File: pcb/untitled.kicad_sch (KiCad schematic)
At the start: 17 parts, among them IC6 AD844_OPAMP_AL, IC7 FOD814_OPTO_AL, J2 Conn_01x03, U3 REF192_AL

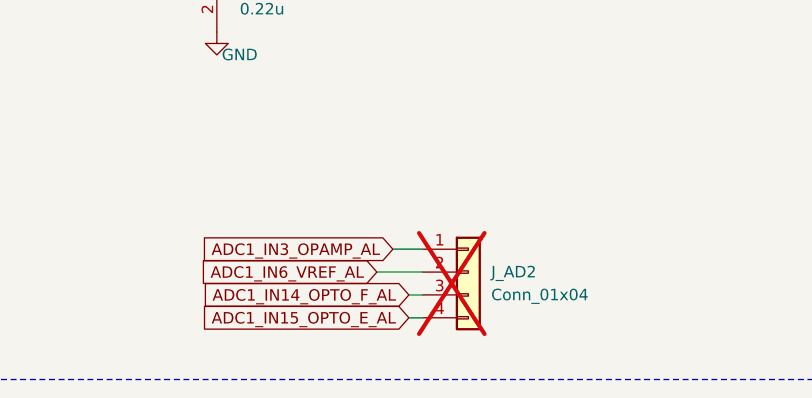
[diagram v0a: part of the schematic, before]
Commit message: Replaced wire to board connectors with screw terminals
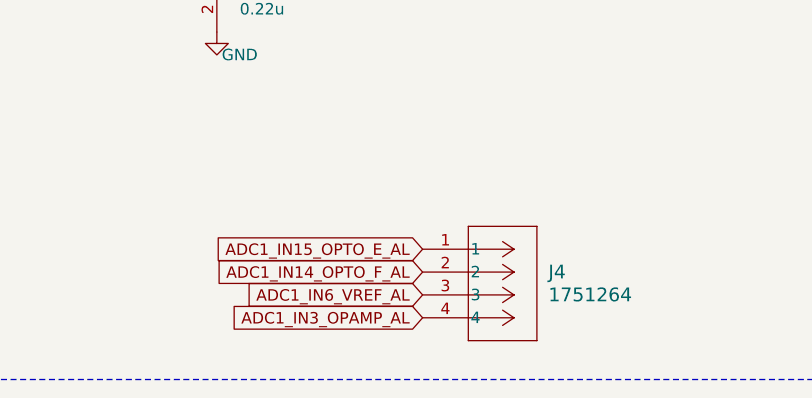
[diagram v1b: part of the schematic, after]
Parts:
- removed J_AD2: Conn_01x04, Connector_PinHeader_2.54mm:PinHeader_1x04_P2.54mm_Vertical, symbol Connector_Generic:Conn_01x04
- added J4: 1751264, Screw Terminal 1x4:CONN_1751264_PXC, symbol Screw Terminal 1x4:1751264
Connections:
- net ADC1_IN14_OPTO_F_AL: now also J4.2
- net ADC1_IN15_OPTO_E_AL: now also J4.1
- net ADC1_IN3_OPAMP_AL: now also J4.4
- net ADC1_IN6_VREF_AL: now also J4.3
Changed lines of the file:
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@@
 	(wire
 		(pts
-			(xy 86.868 147.32) (xy 90.17 147.32)
-		)
-		(stroke
-			(width 0)
-			(type default)
-		)
-	)
-	(wire
-		(pts
 			(xy 292.1 88.9) (xy 292.1 76.2)
 		)
@@
 	(wire
 		(pts
-			(xy 85.09 149.86) (xy 90.17 149.86)
-		)
-		(stroke
-			(width 0)
-			(type default)
-		)
-	)
-	(wire
-		(pts
 			(xy 172.72 93.98) (xy 180.34 93.98)
 		)
@@
 	(wire
 		(pts
-			(xy 88.646 152.4) (xy 90.17 152.4)
-		)
-		(stroke
-			(width 0)
-			(type default)
-		)
-	)
-	(wire
-		(pts
 			(xy 335.28 103.886) (xy 335.28 101.6)
 		)
@@
 	(wire
 		(pts
-			(xy 88.646 154.94) (xy 90.17 154.94)
-		)
-		(stroke
-			(width 0)
-			(type default)
-		)
-	)
-	(wire
-		(pts
 			(xy 58.42 105.41) (xy 76.2 105.41)
 		)
@@
 	(global_label "ADC1_IN15_OPTO_E_AL"
 		(shape input)
-		(at 88.646 154.94 180)
+		(at 90.17 147.32 180)
 		(fields_autoplaced yes)
 		(effects
@@
 		)
 		(property "Intersheetrefs" "${INTERSHEET_REFS}"
-			(at 64.4337 154.94 0)
+			(at 65.9577 147.32 0)
 			(hide yes)
 			(show_name no)
@@
 	(global_label "ADC1_IN14_OPTO_F_AL"
 		(shape input)
-		(at 88.646 152.4 180)
+		(at 90.17 149.86 180)
 		(fields_autoplaced yes)
 		(effects
@@
 		)
 		(property "Intersheetrefs" "${INTERSHEET_REFS}"
-			(at 64.4941 152.4 0)
+			(at 66.0181 149.86 0)
 			(hide yes)
 			(show_name no)
@@
 	(global_label "ADC1_IN6_VREF_AL"
 		(shape input)
-		(at 85.09 149.86 180)
+		(at 90.17 152.4 180)
 		(fields_autoplaced yes)
 		(effects
@@
 		)
 		(property "Intersheetrefs" "${INTERSHEET_REFS}"
-			(at 64.5062 149.86 0)
+			(at 69.5862 152.4 0)
 			(hide yes)
 			(show_name no)
@@
 	(global_label "ADC1_IN3_OPAMP_AL"
 		(shape input)
-		(at 86.868 147.32 180)
+		(at 90.17 154.94 180)
 		(fields_autoplaced yes)
 		(effects
@@
 		)
 		(property "Intersheetrefs" "${INTERSHEET_REFS}"
-			(at 64.4699 147.32 0)
+			(at 67.7719 154.94 0)
 			(hide yes)
 			(show_name no)
@@
 	)
 	(symbol
+		(lib_id "Screw Terminal 1x4:1751264")
+		(at 90.17 147.32 0)
+		(unit 1)
+		(body_style 1)
+		(exclude_from_sim no)
+		(in_bom yes)
+		(on_board yes)
+		(in_pos_files yes)
+		(dnp no)
+		(fields_autoplaced yes)
+		(property "Reference" "J4"
+			(at 104.14 149.8599 0)
+			(show_name no)
+			(do_not_autoplace no)
+			(effects
+				(font
+					(size 1.524 1.524)
+				)
+				(justify left)
+			)
+		)
+		(property "Value" "1751264"
+			(at 104.14 152.3999 0)
+			(show_name no)
+			(do_not_autoplace no)
+			(effects
+				(font
+					(size 1.524 1.524)
+				)
+				(justify left)
+			)
+		)
+		(property "Footprint" "Screw Terminal 1x4:CONN_1751264_PXC"
+			(at 90.17 147.32 0)
+			(hide yes)
+			(show_name no)
+			(do_not_autoplace no)
+			(effects
+				(font
+					(size 1.27 1.27)
+					(italic yes)
+				)
+			)
+		)
+		(property "Datasheet" "1751264"
+			(at 90.17 147.32 0)
+			(hide yes)
+			(show_name no)
+			(do_not_autoplace no)
+			(effects
+				(font
+					(size 1.27 1.27)
+					(italic yes)
+				)
+			)
+		)
+		(property "Description" ""
+			(at 90.17 147.32 0)
+			(hide yes)
+			(show_name no)
+			(do_not_autoplace no)
+			(effects
+				(font
+					(size 1.27 1.27)
+				)
+			)
+		)
+		(pin "1"
+		)
+		(pin "3"
+		)
+		(pin "2"
+		)
+		(pin "4"
+		)
+		(instances
+			(project "mcu_integration"
+				(path "/c0210bc3-f67f-47d8-a34e-f002a728adb2/f1afd235-040c-4b54-9b6d-8df613af2103"
+					(reference "J4")
+					(unit 1)
+				)
+			)
+		)
+	)
+	(symbol
 		(lib_id "Connector_Generic:Conn_01x03")
 		(at 283.21 91.44 180)
@@
 					(unit 1)
 				)
-			)
-		)
-	)
-	(symbol
-		(lib_id "Connector_Generic:Conn_01x04")
-		(at 95.25 149.86 0)
-		(unit 1)
-		(body_style 1)
-		(exclude_from_sim no)
-		(in_bom yes)
-		(on_board yes)
-		(in_pos_files yes)
-		(dnp yes)
-		(fields_autoplaced yes)
-		(property "Reference" "J_AD2"
-			(at 97.79 149.86 0)
-			(show_name no)
-			(do_not_autoplace no)
-			(effects
-				(font
-					(size 1.27 1.27)
-				)
-				(justify left)
-			)
-		)
-		(property "Value" "Conn_01x04"
-			(at 97.79 152.4 0)
-			(show_name no)
-			(do_not_autoplace no)
-			(effects
-				(font
-					(size 1.27 1.27)
-				)
-				(justify left)
-			)
-		)
-		(property "Footprint" "Connector_PinHeader_2.54mm:PinHeader_1x04_P2.54mm_Vertical"
-			(at 95.25 149.86 0)
-			(hide yes)
-			(show_name no)
-			(do_not_autoplace no)
-			(effects
-				(font
-					(size 1.27 1.27)
-				)
-			)
-		)
-		(property "Datasheet" ""
-			(at 95.25 149.86 0)
-			(hide yes)
-			(show_name no)
-			(do_not_autoplace no)
-			(effects
-				(font
-					(size 1.27 1.27)
-				)
-			)
-		)
-		(property "Description" ""
-			(at 95.25 149.86 0)
-			(hide yes)
-			(show_name no)
-			(do_not_autoplace no)
-			(effects
-				(font
-					(size 1.27 1.27)
-				)
-			)
-		)
-		(property "MPN" ""
-			(at 95.25 149.86 0)
-			(hide yes)
-			(show_name no)
-			(do_not_autoplace no)
-			(effects
-				(font
-					(size 1.27 1.27)
-				)
-			)
-		)
-		(property "Manufacturer" ""
-			(at 95.25 149.86 0)
-			(hide yes)
-			(show_name no)
-			(do_not_autoplace no)
-			(effects
-				(font
-					(size 1.27 1.27)
-				)
-			)
-		)
-		(pin "1"
-		)
-		(pin "2"
-		)
-		(pin "3"
-		)
-		(pin "4"
-		)
-		(instances
-			(project "mcu_integration"
-				(path "/c0210bc3-f67f-47d8-a34e-f002a728adb2/f1afd235-040c-4b54-9b6d-8df613af2103"
-					(reference "J_AD2")
-					(unit 1)
-				)
